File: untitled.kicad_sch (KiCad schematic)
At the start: 66 parts, among them U1 K210_C913414, U12 PCIE-67P42H, U4 XC6206P182MR_C347373, U5 GD25LQ128EWIGR, U6 TMI7003C, U7 SGM803-TXN3/TR_C5152602, U8 XC6206P302MR_C347375, X1 X322526MMB4SI

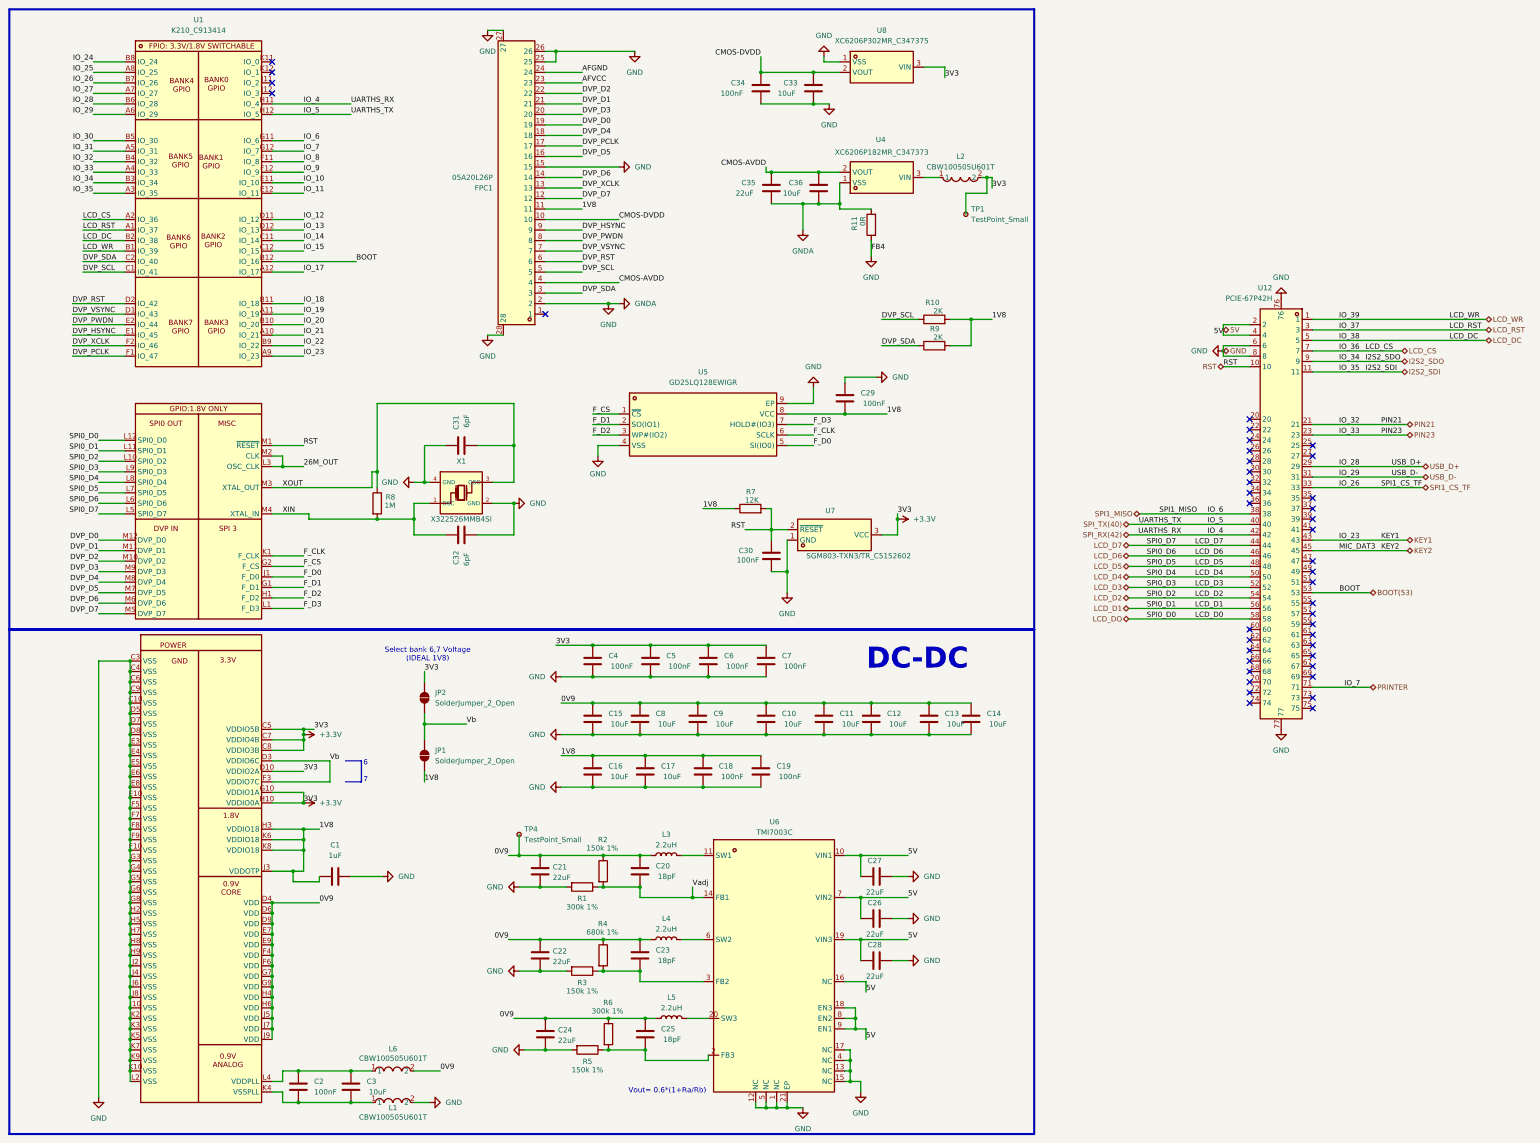
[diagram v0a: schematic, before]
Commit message: troca de resistores por pecas jlcpcb
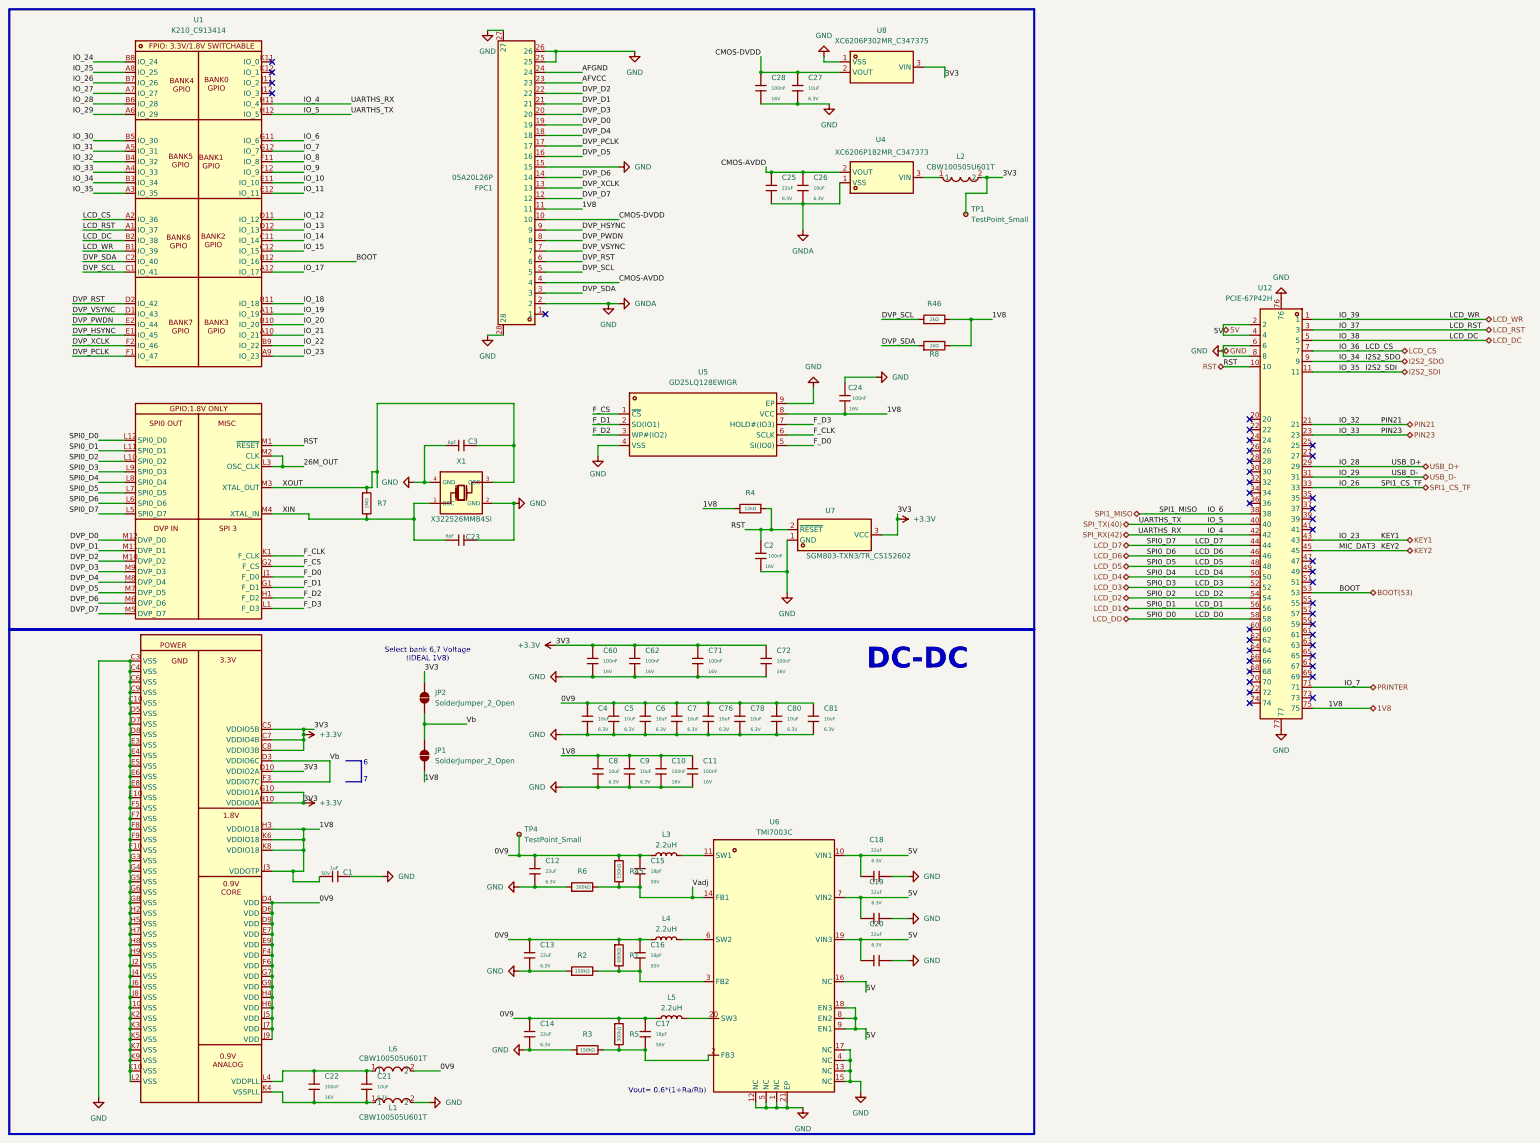
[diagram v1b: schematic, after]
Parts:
- removed C1: 1uF, Capacitor_SMD:C_0201_0603Metric, symbol Device:C
- removed C10, C11, C12, C13, C14, C15, C16, C17, C3, C33, C36, C8, C9: 10uF, Capacitor_SMD:C_0201_0603Metric, symbol Device:C
- removed C18, C19, C2, C29, C30, C34, C4, C5, C6, C7: 100nF, Capacitor_SMD:C_0201_0603Metric, symbol Device:C
- removed C20, C23, C25: 18pF, Capacitor_SMD:C_0201_0603Metric, symbol Device:C
- removed C21, C22, C24, C26, C27, C28, C35: 22uF, Capacitor_SMD:C_0201_0603Metric, symbol Device:C
- removed C31, C32: 6pF, Capacitor_SMD:C_0201_0603Metric, symbol Device:C
- removed R1, R6: 300k 1%, Resistor_SMD:R_0201_0603Metric, symbol Device:R
- removed R10, R9: 2K, Resistor_SMD:R_0201_0603Metric, symbol Device:R
- removed R11: 0R, Resistor_SMD:R_0201_0603Metric, symbol Device:R
- removed R2, R3, R5: 150k 1%, Resistor_SMD:R_0201_0603Metric, symbol Device:R
- removed R4: 680k 1%, Resistor_SMD:R_0201_0603Metric, symbol Device:R
- removed R7: 12K, Resistor_SMD:R_0201_0603Metric, symbol Device:R
- removed R8: 1M, Resistor_SMD:R_0201_0603Metric, symbol Device:R
- added C1: 1uF, PCM_JLCPCB:C_0603, symbol PCM_JLCPCB-Capacitors:0603,1uF
- added C10, C11, C2, C22, C24, C28, C60, C62, C71, C72: 100nF, PCM_JLCPCB:C_0402, symbol PCM_JLCPCB-Capacitors:0402,100nF
- added C12, C13, C14, C18, C19, C20, C25: 22uF, PCM_JLCPCB:C_0603, symbol PCM_JLCPCB-Capacitors:0603,22uF
- added C15, C16, C17: 18pF, PCM_JLCPCB:C_0402, symbol PCM_JLCPCB-Capacitors:0402,18pF
- added C21, C26, C27, C4, C5, C6, C7, C76, C78, C8, C80, C81, C9: 10uF, PCM_JLCPCB:C_0402, symbol PCM_JLCPCB-Capacitors:0402,10uF
- added C23, C3: 6pF, PCM_JLCPCB:C_0402, symbol PCM_JLCPCB-Capacitors:0402,6pF
- added R1: 680kΩ, PCM_JLCPCB:R_0603, symbol PCM_JLCPCB-Resistors:0603,680kΩ
- added R2, R3, R45: 150kΩ, PCM_JLCPCB:R_0402, symbol PCM_JLCPCB-Resistors:0402,150kΩ
- added R4: 12kΩ, PCM_JLCPCB:R_0402, symbol PCM_JLCPCB-Resistors:0402,12kΩ
- added R46, R8: 2kΩ, PCM_JLCPCB:R_0402, symbol PCM_JLCPCB-Resistors:0402,2kΩ
- added R5, R6: 300kΩ, PCM_JLCPCB:R_0402, symbol PCM_JLCPCB-Resistors:0402,300kΩ
- added R7: 1MΩ, PCM_JLCPCB:R_0402, symbol PCM_JLCPCB-Resistors:0402,1MΩ
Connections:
- net +3.3V: now also C60.1, C62.1, C71.1, C72.1
- net 0V9: now also C12.1, C13.1, C14.1, C15.1, C16.1, C17.1, C4.1, C5.1, C6.1, C7.1, C76.1, C78.1, C80.1, C81.1, R1.1, R45.1, R5.1
- net 1V8: now also U12.75, C1.1, C10.1, C11.1, C24.1, C8.1, C9.1, R4.1, R46.2, R8.2
- net 5V: now also C18.1, C19.1, C20.1
- net CMOS-AVDD: now also C25.1, C26.1
- net CMOS-DVDD: now also C27.1, C28.1
- net DVP_SCL: now also R46.1
- net DVP_SDA: now also R8.1
- net GND: now also C1.2, C10.2, C11.2, C12.2, C13.2, C14.2, C18.2, C19.2, C2.1, C20.2, C23.2, C24.2, C25.2, C26.2, C27.2, C28.2, C3.1, C4.2, C5.2, C6.2, C60.2, C62.2, C7.2, C71.2, C72.2, C76.2, C78.2, C8.2, C80.2, C81.2, C9.2, R2.1, R3.1, R6.1
- net RST: now also C2.2, R4.2
- net Vadj: now also C15.2, R45.2, R6.2
- net XIN: now also C23.1, R7.2
- net XOUT: now also C3.2, R7.1
- net at U6.3 (FB2): now also C16.2, R1.2, R2.2
- net at L1.1, U1.K4 (VSSPLL): now also C21.2, C22.2
- net at L6.1, U1.L4 (VDDPLL): now also C21.1, C22.1
- net at U6.2 (FB3): now also C17.2, R3.2, R5.2
- no-connect marks 41 -> 40

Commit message: TROPCAL 01 CONECTIO E ATUALIZACAO E SUBSTITUICAO DE COMPONENTES POR COMPONENTES JLC DISPONIVEIS
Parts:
- removed L3, L4, L5: 2.2uH, Inductor_SMD:L_0805_2012Metric, symbol Device:L
- removed U7: SGM803-TXN3/TR_C5152602, easyeda2kicad:SOT-23-3_L2.9-W1.5-P1.90-LS2.6-BR, symbol easyeda2kicad:SGM803-TXN3_TR_C5152602
- added L3, L4, L8: 2.2uH,50mA, PCM_JLCPCB:L_0805, symbol PCM_JLCPCB-Inductors:2.2uH,50mA
- added U11: APX803-31SAG-7, easyeda2kicad:SOT-23-3_L2.9-W1.3-P1.90-LS2.4-BR, symbol easyeda2kicad:APX803-31SAG-7
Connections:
- net +3.3V: now also U11.3 (VCC)
- net 0V9: now also L3.1, L4.1, L8.1; no longer U1.D6 (VDD), U1.D9 (VDD), U1.E7 (VDD), U1.E9 (VDD), U1.F4 (VDD), U1.F6 (VDD), U1.G7 (VDD), U1.G9 (VDD), U1.H4 (VDD), U1.H6 (VDD), U1.J5 (VDD), U1.J7 (VDD)
- net GND: now also U11.1 (GND); no longer U1.C10 (VSS), U1.C4 (VSS), U1.C6 (VSS), U1.C9 (VSS), U1.D5 (VSS), U1.D7 (VSS), U1.D8 (VSS), U1.E10 (VSS), U1.E3 (VSS), U1.E4 (VSS), U1.E5 (VSS), U1.E6 (VSS), U1.E8 (VSS), U1.F10 (VSS), U1.F5 (VSS), U1.F7 (VSS), U1.F8 (VSS), U1.F9 (VSS), U1.G3 (VSS), U1.G4 (VSS), U1.G5 (VSS), U1.G6 (VSS), U1.G8 (VSS), U1.H2 (VSS), U1.H5 (VSS), U1.H7 (VSS), U1.H8 (VSS), U1.H9 (VSS), U1.J10 (VSS), U1.J2 (VSS), U1.J4 (VSS), U1.J6 (VSS), U1.J8 (VSS), U1.K10 (VSS), U1.K2 (VSS), U1.K3 (VSS), U1.K5 (VSS), U1.K7 (VSS), U1.K9 (VSS)
- net IO_11: now also U12.67
- net IO_13: now also U12.63
- net IO_15: now also U12.59
- net IO_17: now also U12.55
- net IO_9: now also U12.69
- net RST: now also U11.2 (~{RESET})
- net at U6.20 (SW3): now also L4.2
- net at U6.6 (SW2): now also L3.2
- net at U6.11 (SW1): now also L8.2
- no-connect marks 40 -> 35
